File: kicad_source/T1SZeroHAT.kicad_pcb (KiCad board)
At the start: 2 copper layers, 65 x 30 mm, 35 parts, among them CN1 RASPI-IO, CN2 XY2500R-F-3.81-4P, CN3 SM04B-GHS-TB, CN4 SM04B-GHS-TB, SW1 SS-3235S-L3, U1 MCP2518FDT-E/SL, U2 TCAN332GDR, Y1 X1E0000210808

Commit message: made first draft of layout
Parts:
- removed D1: MBR0530T, Diode_SMD:D_SOD-123
- removed D2: 19-217/GHC-YR1S2/3T, LED_SMD:LED_0603_1608Metric
- removed D3: KT-0603R, LED_SMD:LED_0603_1608Metric
- removed D4: 19-213/Y2C-CQ2R2L/3T(CY), LED_SMD:LED_0603_1608Metric
- removed F1: nSMD050-33V, Fuse:Fuse_1206_3216Metric
- removed U2: TCAN332GDR, Package_SO:SOIC-8_3.9x4.9mm_P1.27mm
- added C10: 100nF, Capacitor_SMD:C_0603_1608Metric, F.Cu at (134.5, 97.0)
- added C11: 220nF, Capacitor_SMD:C_0603_1608Metric, F.Cu at (128.0, 106.4)
- added C12: 220nF, Capacitor_SMD:C_0603_1608Metric, F.Cu at (119.0, 106.4)
- added C5: 4.7 uF, Capacitor_SMD:C_0603_1608Metric, F.Cu at (136.0, 97.0)
- added C6: 100nF, Capacitor_SMD:C_0603_1608Metric, F.Cu at (137.5, 97.0)
- added C7: 100nF, Capacitor_SMD:C_0603_1608Metric, F.Cu at (139.0, 97.0)
- added C8: 100nF, Capacitor_SMD:C_0603_1608Metric, F.Cu at (122.7, 101.6)
- added C9: 100nF, Capacitor_SMD:C_0603_1608Metric, F.Cu at (124.3, 101.6)
- added FL1: Filter_EMI_CommonMode, Filter:Filter_Bourns_SRF0905_6.0x9.2mm, F.Cu at (121.3, 96.3)
- added R14: 0R, Resistor_SMD:R_0603_1608Metric, F.Cu at (133.6, 94.6)
- added R15: 10k, Resistor_SMD:R_0603_1608Metric, F.Cu at (125.0, 103.9)
- added R16: 10k, Resistor_SMD:R_0603_1608Metric, F.Cu at (122.0, 103.9)
- added R17: 49R9, Resistor_SMD:R_0603_1608Metric, F.Cu at (122.0, 106.4)
- added R18: DNI, Resistor_SMD:R_0603_1608Metric, F.Cu at (121.3, 95.0)
- added R19: DNI, Resistor_SMD:R_0603_1608Metric, F.Cu at (121.3, 97.6)
- CN2: value XY2500R-F-3.81-4P -> XY2500R-F-3.81-2P; footprint Connector_Phoenix_MC:PhoenixContact_MC_1,5_4-G-3.81_1x04_P3.81mm_Horizontal -> Connector_Phoenix_MC:PhoenixContact_MC_1,5_2-G-3.81_1x02_P3.81mm_Horizontal
- CN3, CN4: value SM04B-GHS-TB -> SM02B-GHS-TB; footprint Connector_JST:JST_GH_SM04B-GHS-TB_1x04-1MP_P1.25mm_Horizontal -> Connector_JST:JST_GH_SM02B-GHS-TB_1x02-1MP_P1.25mm_Horizontal
- R10, R11: value 2k2 -> 0R
- R12: value 10k -> 12k4
- R4: value 120R -> 49R9
- U1: value MCP2518FDT-E/SL -> LAN8651; footprint Package_SO:SOIC-14_3.9x8.7mm_P1.27mm -> Package_DFN_QFN:QFN-32-1EP_5x5mm_P0.5mm_EP3.45x3.45mm
- moved R12 31.0 mm to (132.8, 97.0), turned to 90 degrees
- moved C1 17.3 mm to (137.7, 107.2), turned to -90 degrees
- moved R11 15.0 mm to (139.3, 107.2)
- moved C4 13.2 mm to (129.8, 103.3), turned to 180 degrees
- moved R10 10.6 mm to (133.7, 107.2), turned to -90 degrees
- moved C2 10.3 mm to (129.8, 96.0), turned to 0 degrees
- moved R4 6.95 mm to (125.0, 106.4), turned to 0 degrees
- moved Y1 4.47 mm to (129.8, 98.9), turned to -90 degrees
- moved CN2 3.67 mm to (121.5, 109.8)
- moved C3 1.70 mm to (129.8, 101.8), turned to 180 degrees
- moved U1 1.10 mm to (136.5, 101.9), turned to 90 degrees
- moved D5 0.06 mm to (134.8, 113.1)
- turned SW1 to 90 degrees
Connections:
- C4 pad 1: +3.3V -> /VDDA
- CN2 pad 1: GND -> /TRXP
- CN2 pad 2: /CANL -> /TRXN
- CN3 pad 1: /CANVCC -> /TRXP
- CN3 pad 2: /CANH -> /TRXN
- CN4 pad 1: /CANVCC -> /TRXP
- CN4 pad 2: /CANH -> /TRXN
- D5 pad 1: /CANH -> /TRXN
- D5 pad 2: /CANL -> /TRXP
- R1 pad 2: /MCP2517_CS -> /LAN8651_CS
- R10 pad 1: /CAN_RX -> /LAN8651_WAKE_IN
- R10 pad 2: Net-(D2-Pad1) -> GND
- R11 pad 1: /CAN_TX -> +3.3V
- R11 pad 2: Net-(D3-Pad1) -> /LAN8651_RESET_N
- R12 pad 1: /CANVCC -> /RBIAS
- R12 pad 2: Net-(D4-Pad2) -> GND
- R2 pad 1: /MCP2517_CS -> /LAN8651_CS
- R3 pad 2: /MCP2517_CS -> /LAN8651_CS
- R4 pad 1: /CANH -> /TRXN
- R4 pad 2: Net-(R4-Pad2) -> Net-(C11-Pad1)
- R5 pad 2: /MCP2517_INT -> /LAN8651_INT
- R6 pad 2: /MCP2517_INT -> /LAN8651_INT
- R7 pad 2: /MCP2517_INT -> /LAN8651_INT
- R8 pad 2: /MCP2517_INT -> /LAN8651_INT
- R9 pad 2: /MCP2517_INT -> /LAN8651_INT
- SW1 pad 1: Net-(R4-Pad2) -> Net-(C11-Pad2)
- SW1 pad 2: /CANL -> GND
- SW1 pad 4: unconnected-(SW1-Pad4) -> Net-(C12-Pad2)
- SW1 pad 5: unconnected-(SW1-Pad5) -> GND
- U1 pad 1: /CAN_TX -> unconnected-(U1-Pad1)
- U1 pad 10: /SPI_CLK -> /SPI_MISO
- U1 pad 11: /SPI_MOSI -> /LAN8651_CS
- U1 pad 12: /SPI_MISO -> /SPI_CLK
- U1 pad 13: /MCP2517_CS -> /SPI_MOSI
- U1 pad 14: +3.3V -> unconnected-(U1-Pad14)
- U1 pad 2: /CAN_RX -> GND
- U1 pad 3: unconnected-(U1-Pad3) -> GND
- U1 pad 4: /MCP2517_INT -> +3.3V
- U1 pad 5: /OSC2 -> GND
- U1 pad 6: /OSC1 -> unconnected-(U1-Pad6)
- U1 pad 7: GND -> +3.3V
- U1 pad 8: unconnected-(U1-Pad8) -> /LAN8651_RESET_N
- U1 pad 9: unconnected-(U1-Pad9) -> /LAN8651_INT
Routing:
- net GND: track 200.8 -> 113.1 mm, vias 24 -> 19
- net /CANL: track 55.4 -> 0.00 mm
- net /CANH: track 50.1 -> 0.00 mm
- net /TRXN: track 0.00 -> 48.4 mm
- net /TRXP: track 0.00 -> 47.5 mm
- net +5V: track 37.4 -> 2.54 mm
- net /CANVCC: track 34.1 -> 0.00 mm
- net /LAN8651_INT: track 0.00 -> 30.7 mm
- net /MCP2517_INT: track 30.1 -> 0.00 mm, vias 2 -> 0
- net /CAN_RX: track 25.2 -> 0.00 mm
- net Net-(C11-Pad2): track 0.00 -> 21.7 mm, vias 0 -> 2
- net /TRXP_C: track 0.00 -> 20.2 mm
- net /TRXN_C: track 0.00 -> 18.0 mm
- net /TRXP_I: track 0.00 -> 17.1 mm
- net /LAN8651_CS: track 0.00 -> 14.6 mm, vias 0 -> 2
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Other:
- board text added: "T1SZeroHAT 0.1"
- board text added: "T1Sin"
- board text added: "T1Sout"
- board text added: "TRX+"
- board text added: "TRX-"
- board text removed: "CANFDZeroHAT 0.3"
- board text removed: "CANH"
- board text removed: "CANL"
- board text removed: "CANVCC"
- board text removed: "CANin"
- board text removed: "CANout"
- board text removed: "GND"
- board text removed: "VCC"

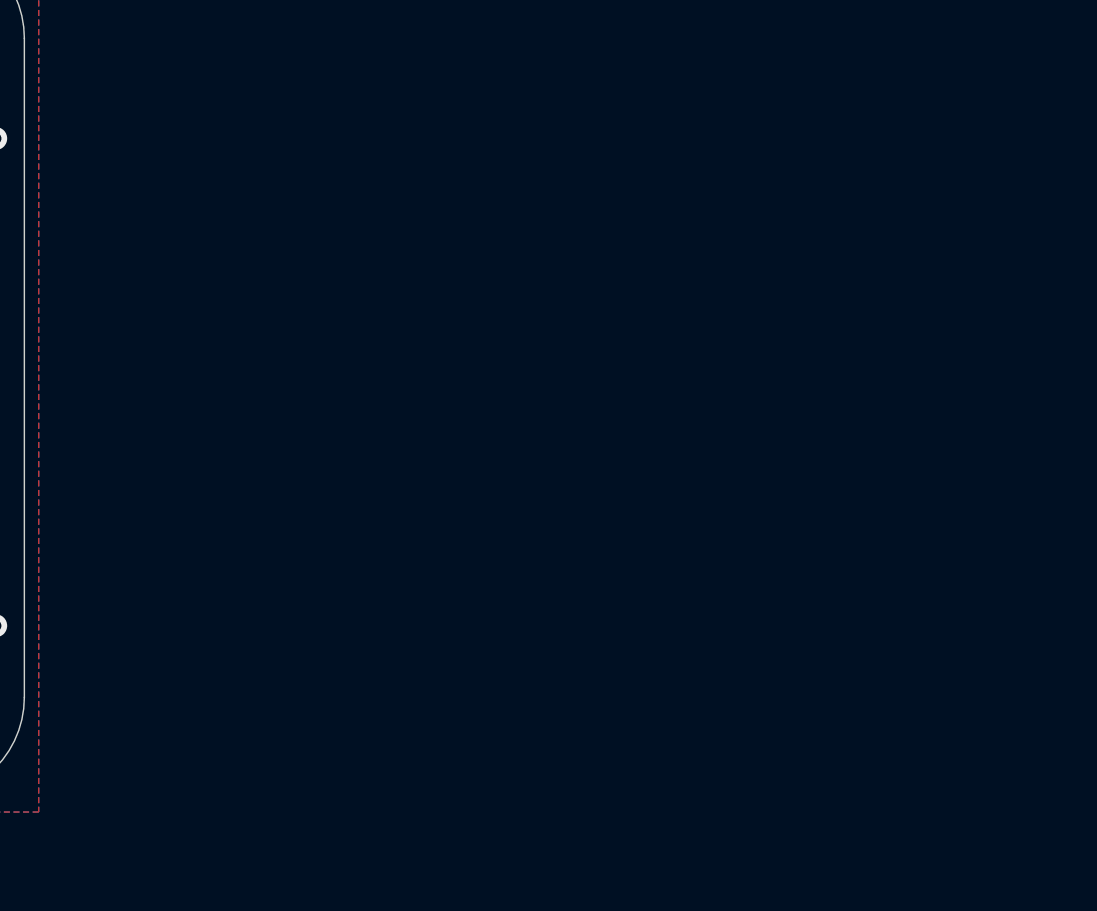
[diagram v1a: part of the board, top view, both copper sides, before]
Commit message: updated schematic for power delivery
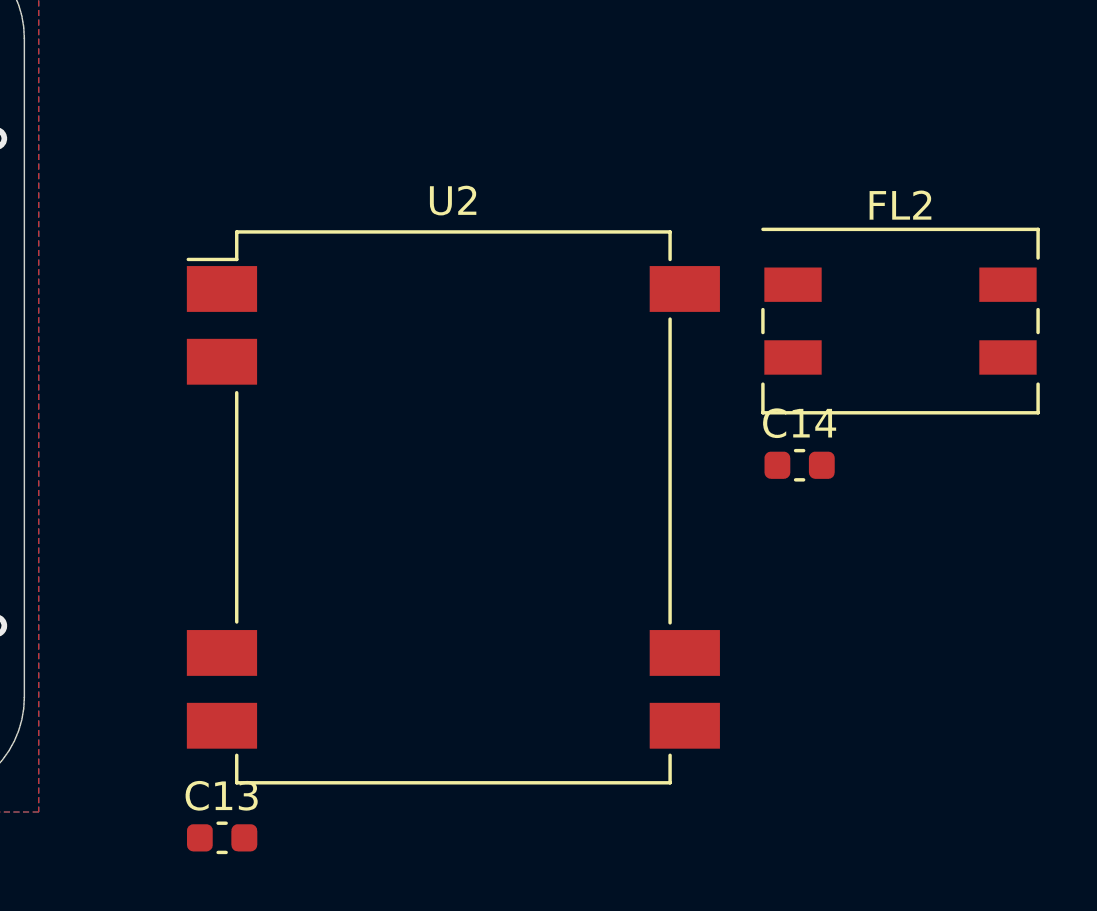
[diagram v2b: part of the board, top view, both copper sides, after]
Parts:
- added C13: 4.7 uF, Capacitor_SMD:C_0603_1608Metric, F.Cu at (179.4, 117.9)
- added C14: 4.7 uF, Capacitor_SMD:C_0603_1608Metric, F.Cu at (199.6, 104.9)
- added FL2: Filter_EMI_CommonMode, Filter:Filter_Bourns_SRF0905_6.0x9.2mm, F.Cu at (203.1, 99.9)
- added U2: ISU0205S12, Converter_DCDC:Converter_DCDC_XP_POWER-ISU02_SMD, F.Cu at (187.5, 106.4)

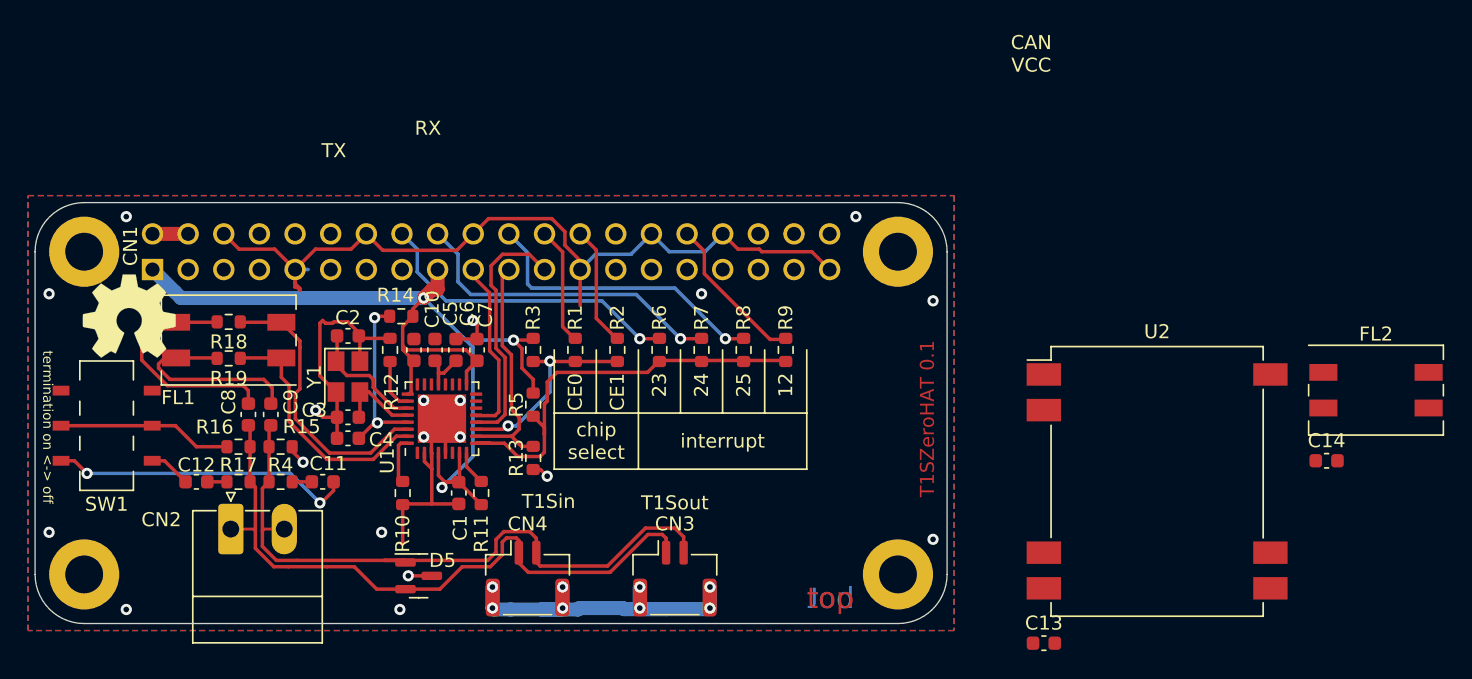
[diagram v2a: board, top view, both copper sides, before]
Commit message: updated layout for power delivery
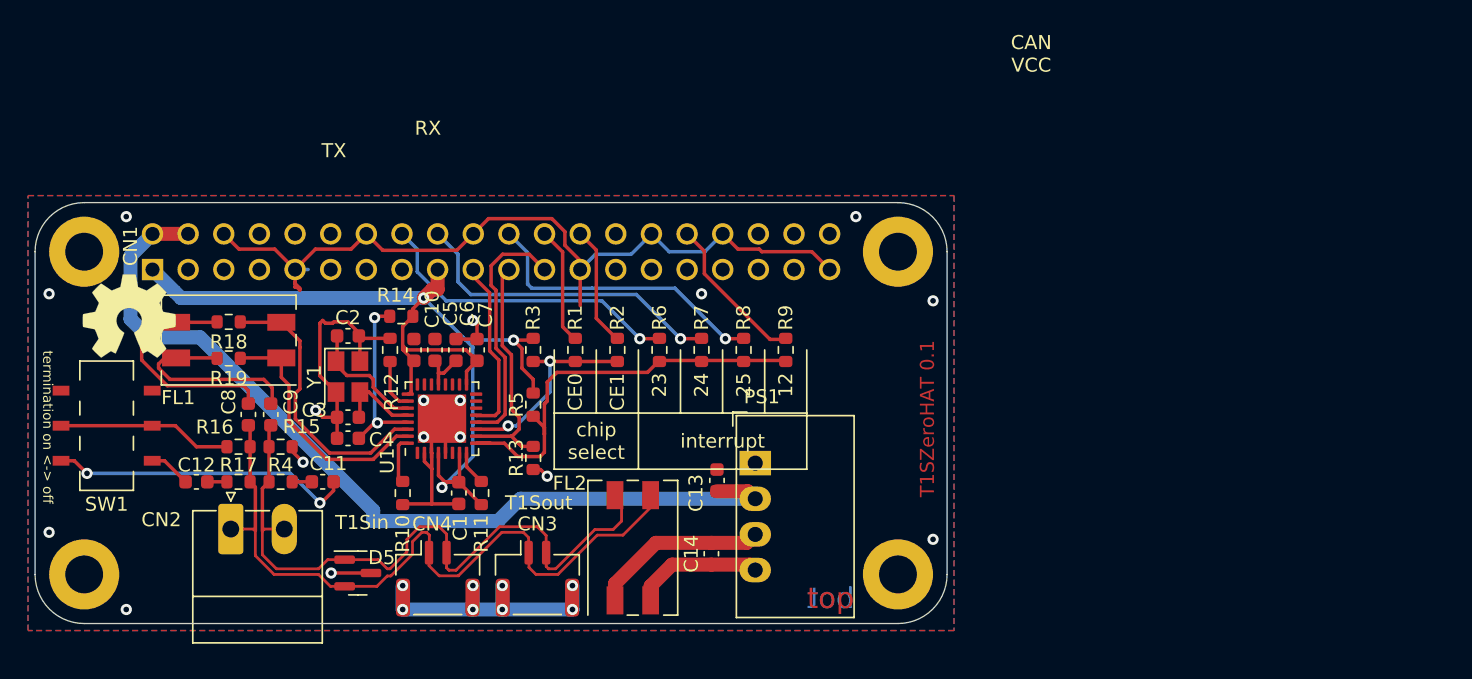
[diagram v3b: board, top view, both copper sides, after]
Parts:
- removed U2: ISU0205S12, Converter_DCDC:Converter_DCDC_XP_POWER-ISU02_SMD
- added PS1: MEE3S0512SC, Converter_DCDC:Converter_DCDC_Murata_MEE3SxxxxSC_THT, F.Cu at (158.8, 105.1)
- moved FL2 54.1 mm to (150.1, 111.1), turned to 90 degrees
- moved C14 44.3 mm to (155.7, 111.5), turned to 90 degrees
- moved C13 26.0 mm to (156.1, 106.3), turned to 90 degrees
- moved CN3 9.80 mm to (143.3, 113.3)
- moved CN4 6.40 mm to (136.2, 113.3)
- moved D5 4.34 mm to (130.5, 112.9)
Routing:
- net +5V: track 2.54 -> 63.8 mm
- net /TRXN_P: track 0.00 -> 12.6 mm
- net /TRXP_P: track 0.00 -> 9.27 mm
- net /MP: track 25.1 -> 18.9 mm
- net /TRXP: track 47.5 -> 51.7 mm
- net GND: track 113.1 -> 111.5 mm, vias 19 -> 17
- net /TRXN: track 48.4 -> 49.4 mm

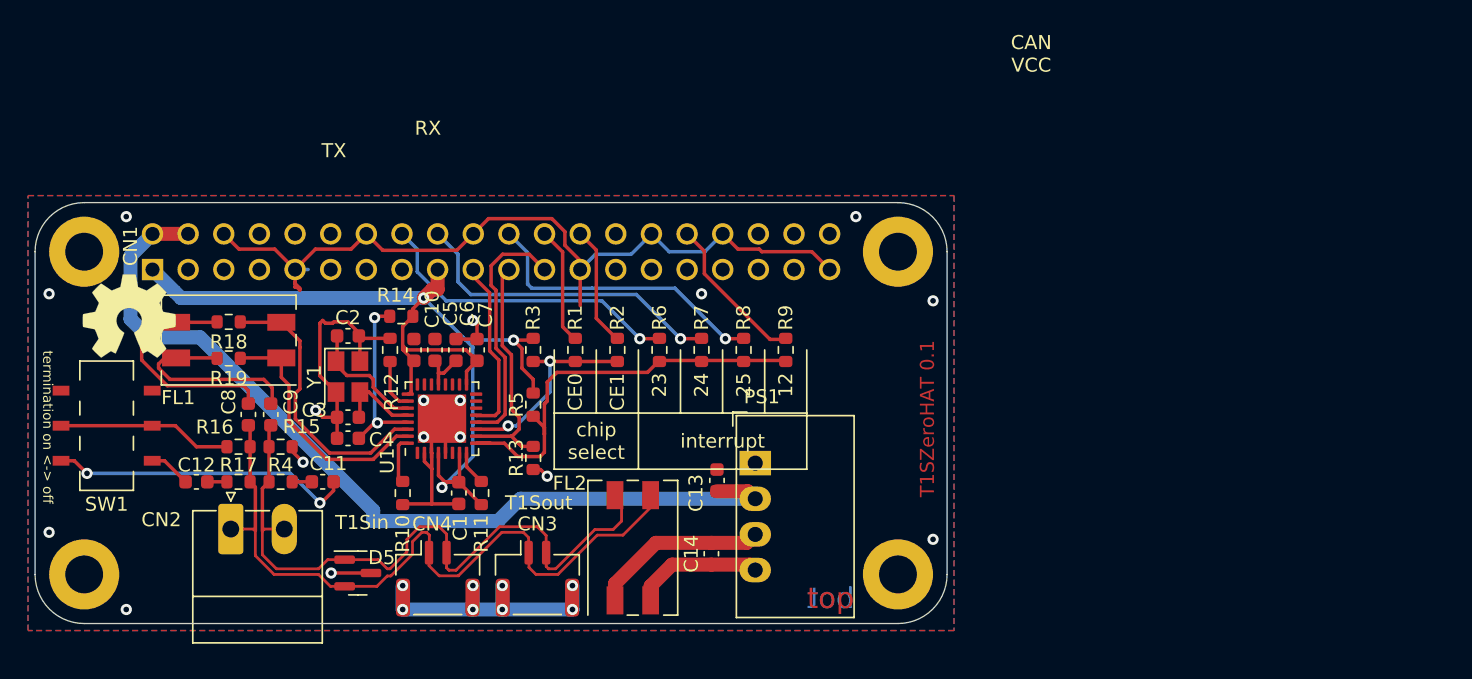
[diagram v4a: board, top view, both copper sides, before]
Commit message: removed power delivery parts since they are not specified
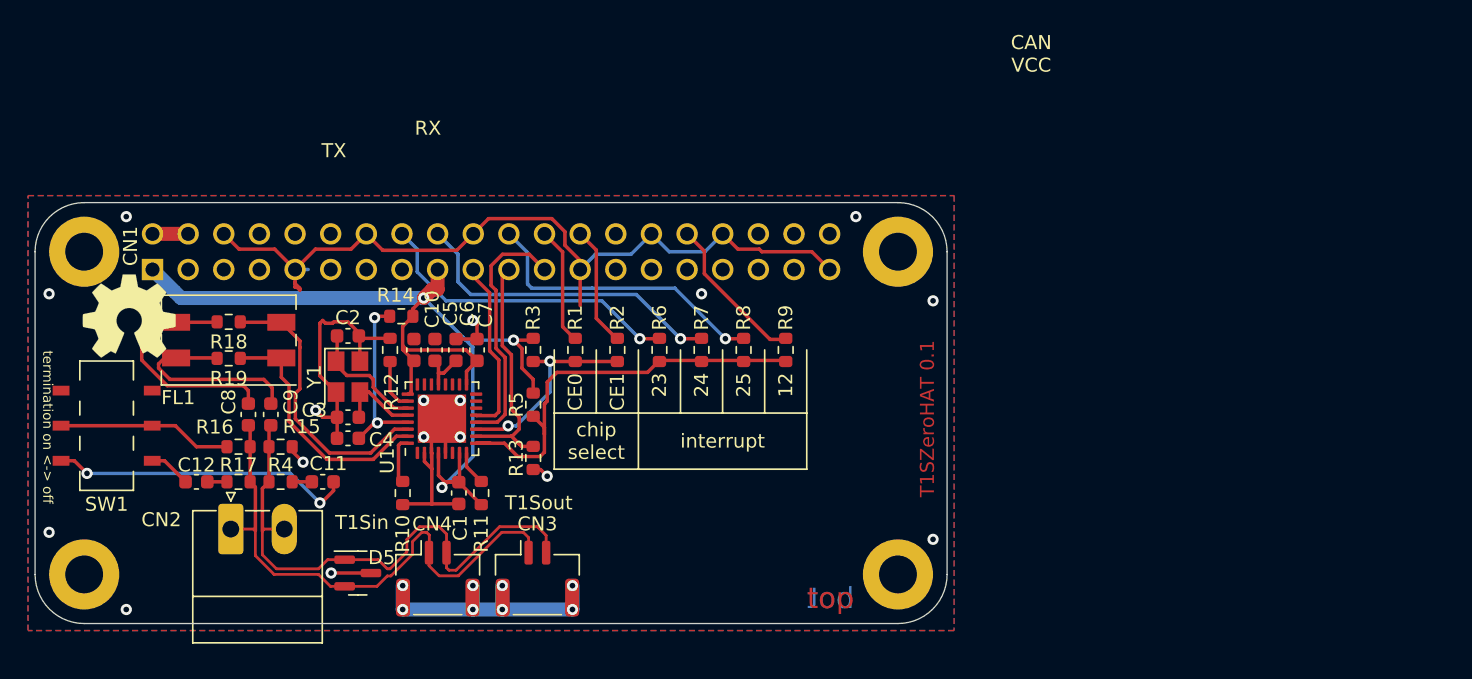
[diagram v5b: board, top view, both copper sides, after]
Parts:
- removed C13, C14: 4.7 uF, Capacitor_SMD:C_0603_1608Metric
- removed FL2: Filter_EMI_CommonMode, Filter:Filter_Bourns_SRF0905_6.0x9.2mm
- removed PS1: MEE3S0512SC, Converter_DCDC:Converter_DCDC_Murata_MEE3SxxxxSC_THT
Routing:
- net +5V: track 63.8 -> 2.54 mm
- net /TRXP: track 51.7 -> 38.9 mm
- net /TRXN_P: track 12.6 -> 0.00 mm
- net /TRXN: track 49.4 -> 39.5 mm
- net /TRXP_P: track 9.27 -> 0.00 mm
